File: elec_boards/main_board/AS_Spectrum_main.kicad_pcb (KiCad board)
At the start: 2 copper layers, 171.2 x 125 mm, 59 parts, among them J1 MODE, J10 Morpho_Gauche, J11 RN42X-DROITE, J12 POW-5V, J13 Bande1, J14 Morpho_Droite, J15 Lidar, J16 Bande2, J17 Bande3, J18 GND_reg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

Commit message: Update Main Board Schematic and PCB
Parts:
- added G***: LOGO, Logos:logo_lense, F.Cu at (69.1, 121.4)
- moved R4 252.6 mm to (78.2, 138.7), turned to 270 degrees
- moved D7 213.5 mm to (81.3, 86.9), turned to 90 degrees
- moved D3 201.0 mm to (85.9, 70.6)
- moved D8 186.8 mm to (84.3, 79.2), turned to 270 degrees
- moved D4 182.5 mm to (93.5, 73.7), turned to 180 degrees
- moved D1 179.8 mm to (82.3, 148.8), turned to 90 degrees
- moved D2 175.9 mm to (85.9, 141.2), turned to 270 degrees
- moved R7 163.3 mm to (77.2, 76.7), turned to 270 degrees
- moved R5 148.1 mm to (96.0, 67.1), turned to 180 degrees
- moved D10 146.1 mm to (149.9, 73.7), turned to 180 degrees
- moved D9 144.1 mm to (142.2, 70.6)
- moved R6 135.9 mm to (208.8, 67.1), turned to 180 degrees
- moved R8 105.1 mm to (152.4, 67.1), turned to 180 degrees
- moved D6 92.6 mm to (206.2, 73.7), turned to 180 degrees
- moved J2 85.1 mm to (105.2, 165.6)
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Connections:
- J10 pad 15: MISC -> Net-(J10-Pad15)
- J10 pad 17: COLORS -> Net-(J10-Pad17)
- J10 pad 19: MODE -> Net-(J10-Pad19)
- J10 pad 30: NUC_B1 -> NUC_B4.5
- J10 pad 32: NUC_B2 -> NUC_B5
- J10 pad 34: NUC_B3 -> Net-(J10-Pad34)
- J10 pad 36: NUC_B4 -> Net-(J10-Pad36)
- J10 pad 37: LUM -> NUC_B4
- J10 pad 38: NUC_B4.5 -> NUC_B1
- J10 pad 39: NUC_B6 -> NUC_B3
- J10 pad 40: NUC_B5 -> NUC_B2
- J14 pad 14: Net-(J14-Pad14) -> MISC
- J14 pad 16: Net-(J14-Pad16) -> COLORS
- J14 pad 18: Net-(J14-Pad18) -> MODE
- J14 pad 19: IRQ_nRF -> CE_nRF
- J14 pad 26: Net-(J14-Pad26) -> LUM
- J14 pad 3: CSN_nRF -> Net-(J14-Pad3)
- J14 pad 35: Net-(J14-Pad35) -> IRQ_nRF
- J14 pad 5: CE_nRF -> Net-(J14-Pad5)
- J14 pad 7: Net-(J14-Pad7) -> CSN_nRF
- J14 pad 8: Net-(J14-Pad8) -> NUC_B6
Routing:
- net +12V: track 0.00 -> 673.7 mm, vias 0 -> 15
- net 3.3V_NUC: track 0.00 -> 648.5 mm, vias 0 -> 15
- net -12V: track 0.00 -> 595.8 mm
- net Micro: track 0.00 -> 376.7 mm, vias 0 -> 10
- net 5V_NUC: track 0.00 -> 189.8 mm, vias 0 -> 7
- net NUC_B5: track 0.00 -> 117.4 mm
- net NUC_B4.5: track 0.00 -> 115.5 mm
- net CSN_nRF: track 0.00 -> 106.5 mm
- net NUC_B1: track 0.00 -> 99.1 mm
- net MOSI: track 4.21 -> 87.7 mm, vias 0 -> 2
- net NUC_B2: track 0.00 -> 81.2 mm
- net MISO: track 0.00 -> 69.8 mm, vias 0 -> 2
- net SCK: track 2.49 -> 69.3 mm
- net CE_nRF: track 0.00 -> 59.1 mm
- net LED_1: track 0.00 -> 58.0 mm
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- added copper zone on B.Cu, net GND
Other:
- board size 171.2 x 125 mm -> 171.2 x 126 mm
- board text added: "+12V"
- board text added: "+3.3V"
- board text added: "+5V"
- board text added: "-12V"
- board text added: "5V"
- board text added: "BAND 1"
- board text added: "BAND 2"
- board text added: "BAND 3"
- board text added: "BAND 4"
- board text added: "BAND 4.5"
- board text added: "BAND 5"
- board text added: "BAND 6"
- board text added: "CHOICE"
- board text added: "D_out"
- board text added: "IN"
- board text added: "JACK"
- board text added: "LED_Strip"
- board text added: "LIDAR"
- board text added: "LUMINOSITE"
- board text added: "MIC"
- board text added: "MICRO"
- board text added: "MIC_IN"
- board text added: "OUT"
- board text added: "RX"
- board text added: "TX"
- board text added: "VOLUME"
- board text removed: "3.3V"

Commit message: Update Schematics and PCB
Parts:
- moved G*** 54.0 mm to (105.2, 81.3), turned to 0 degrees
- renumbered REF** to MH
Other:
- board text added: "Nucleo / L476RG"

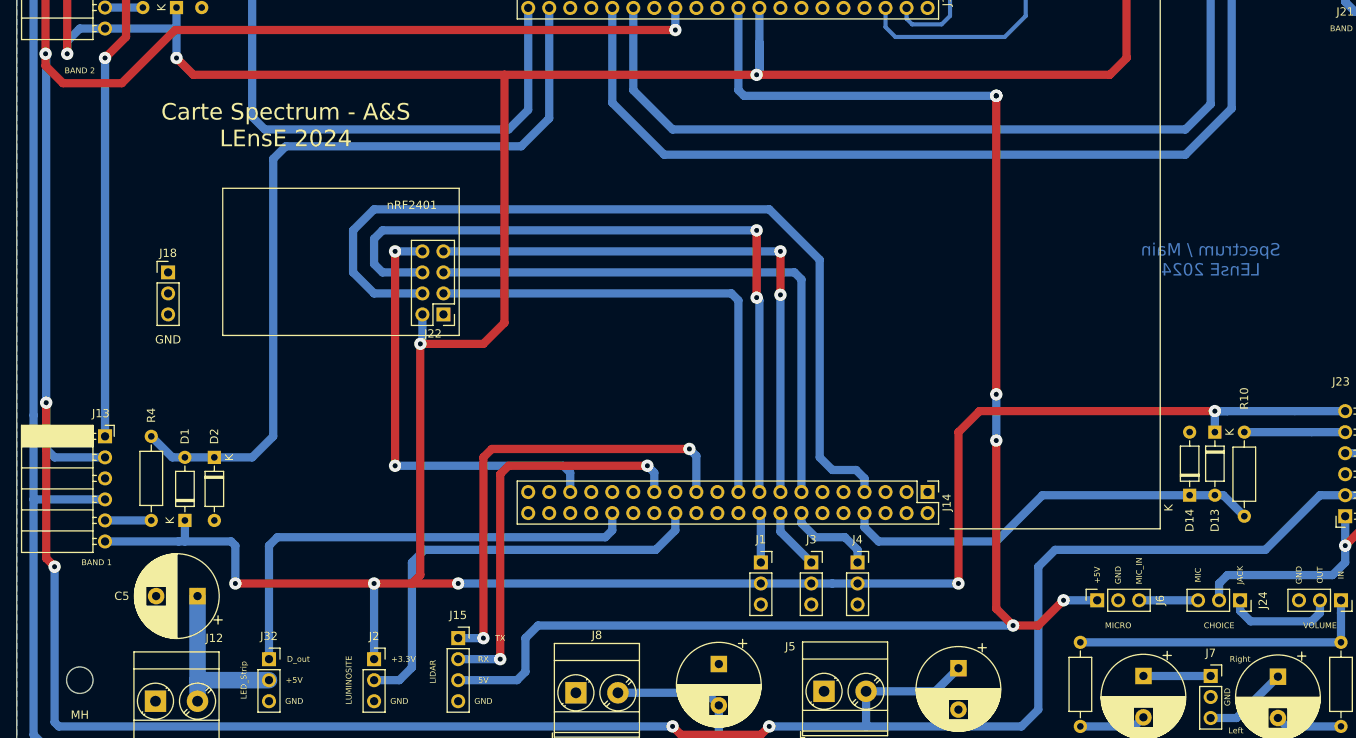
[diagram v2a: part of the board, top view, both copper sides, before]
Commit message: Update Schematics and PCB - Adding LEDs
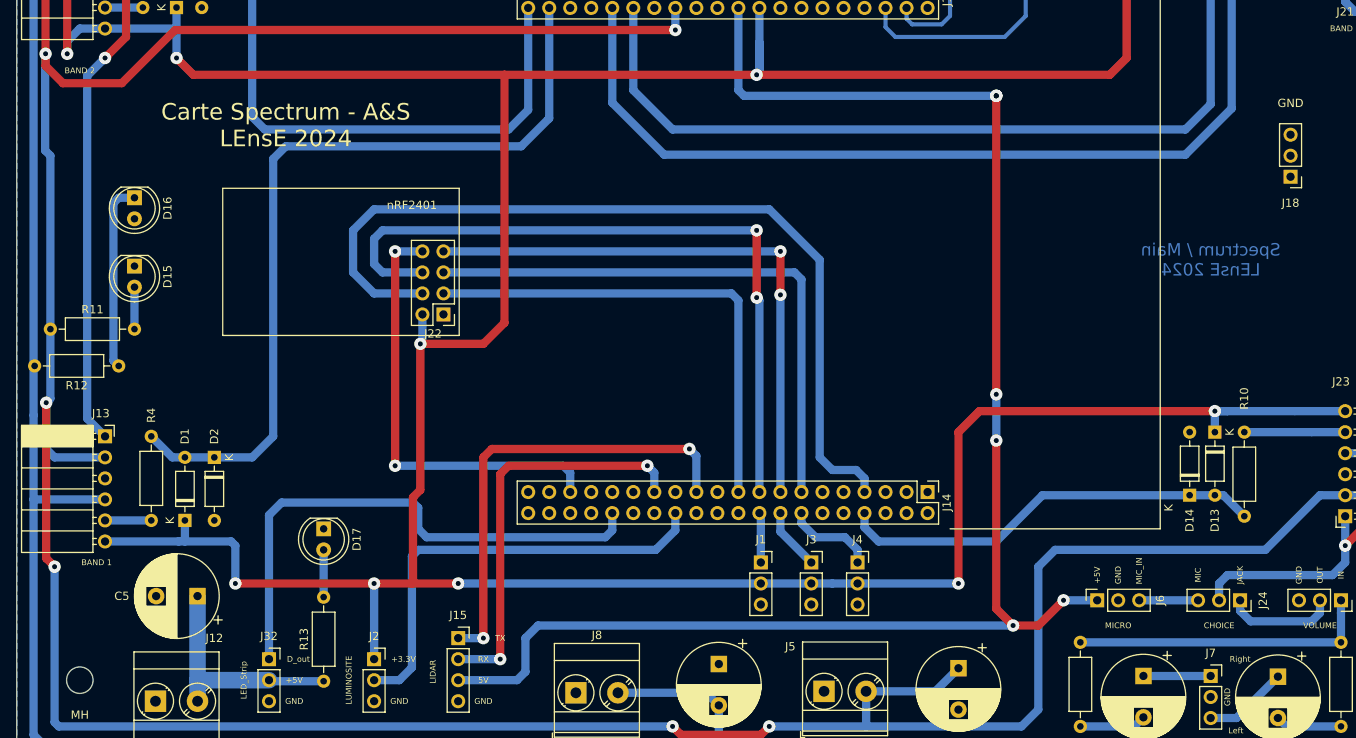
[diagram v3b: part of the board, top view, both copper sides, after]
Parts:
- added D15: LED_12V, LED_THT:LED_D5.0mm_FlatTop, F.Cu at (76.2, 118.1)
- added D16: LED_-12V, LED_THT:LED_D5.0mm_FlatTop, F.Cu at (76.2, 109.9)
- added D17: LED_5V, LED_THT:LED_D5.0mm_FlatTop, F.Cu at (99.1, 149.9)
- added R11: 560, Resistor_THT:R_Axial_DIN0207_L6.3mm_D2.5mm_P10.16mm_Horizontal, F.Cu at (66.0, 125.7)
- added R12: 560, Resistor_THT:R_Axial_DIN0207_L6.3mm_D2.5mm_P10.16mm_Horizontal, F.Cu at (74.3, 130.2)
- added R13: 220, Resistor_THT:R_Axial_DIN0207_L6.3mm_D2.5mm_P10.16mm_Horizontal, F.Cu at (99.1, 168.3)
- moved J18 136.1 mm to (215.9, 107.3), turned to 180 degrees
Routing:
- net Net-(D16-Pad1): track 0.00 -> 22.7 mm
- net LED_1: track 58.0 -> 65.2 mm
- net 5V_POW: track 21.3 -> 28.0 mm
- net Net-(D17-Pad2): track 0.00 -> 5.72 mm
- net Net-(D15-Pad2): track 0.00 -> 5.08 mm
- net Micro: track 376.7 -> 378.5 mm
